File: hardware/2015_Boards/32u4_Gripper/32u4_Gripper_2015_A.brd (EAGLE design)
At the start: 31.8 x 55.9 mm, 20 parts, among them U1 SN74LS241DW, U2 XBEE-1B3

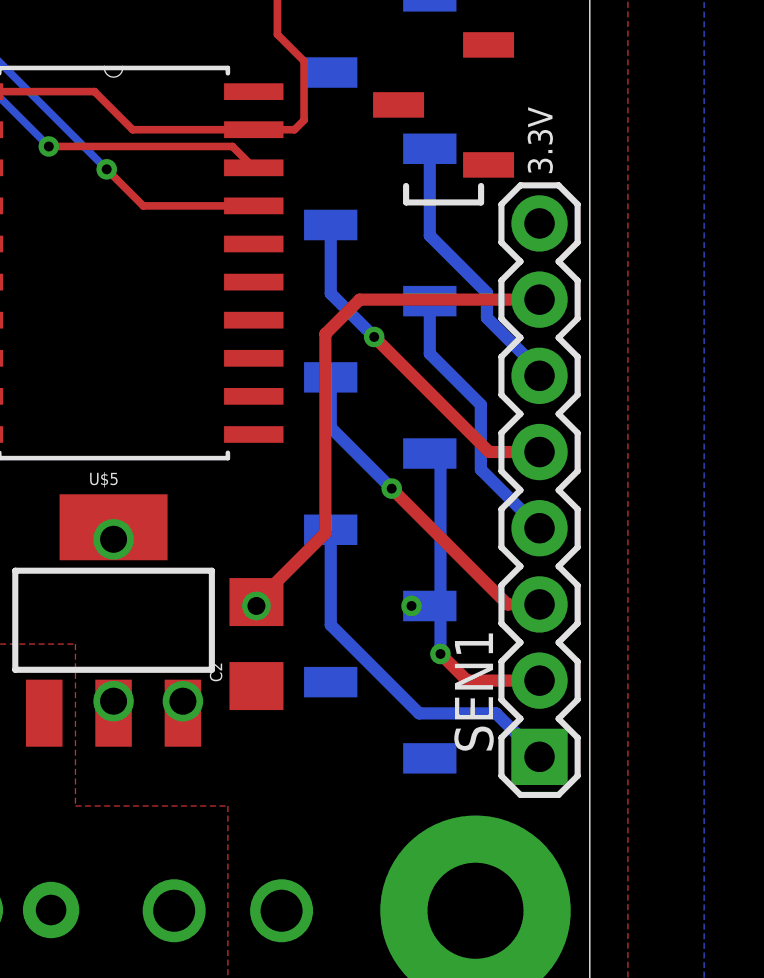
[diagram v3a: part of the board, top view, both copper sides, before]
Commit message: Cleaned up servo data trace
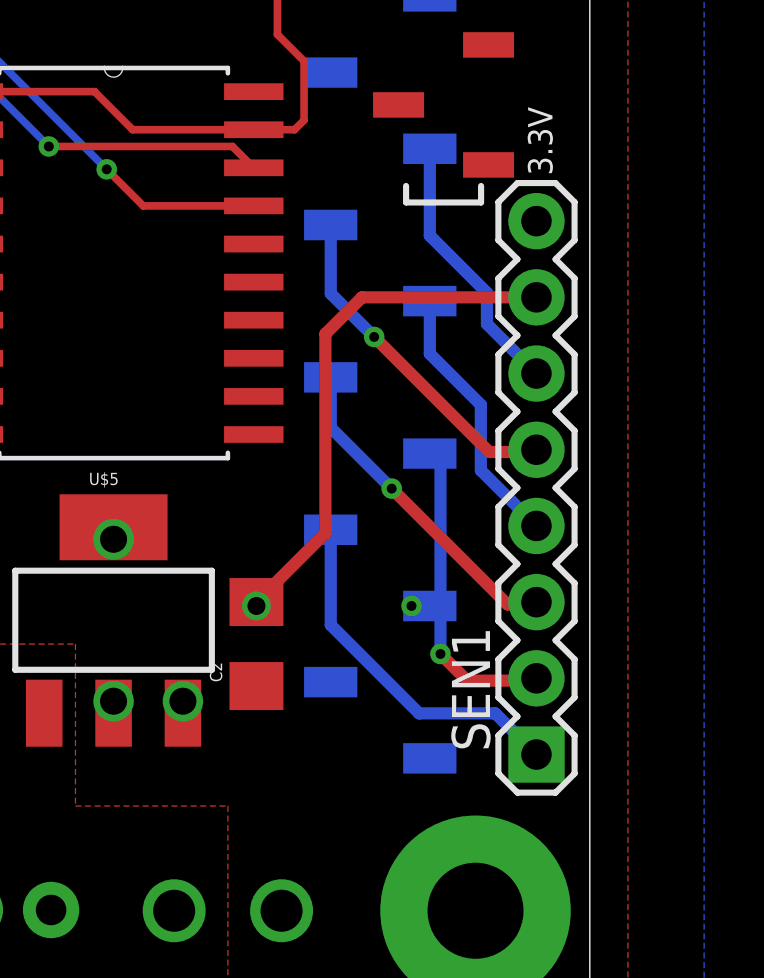
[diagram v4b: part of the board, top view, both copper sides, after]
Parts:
- moved SEN1 0.13 mm to (30.0, 9.02)
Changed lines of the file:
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@@
 <element name="C1" library="SparkFun-Passives" package="1206" value="0.1uF" x="11.1125" y="12.7" rot="R90"/>
 <element name="C2" library="SparkFun-Passives" package="1206" value="0.1uF" x="20.6375" y="12.7" rot="R90"/>
-<element name="SEN1" library="SparkFun-Connectors" package="1X08" value="" x="30.0736" y="8.9408" smashed="yes" rot="R90">
-<attribute name="NAME" x="28.5242" y="9.0424" size="1.27" layer="25" ratio="10" rot="R90"/>
-<attribute name="VALUE" x="33.2486" y="7.6708" size="1.27" layer="27" rot="R90"/>
+<element name="SEN1" library="SparkFun-Connectors" package="1X08" value="" x="29.972" y="9.017" smashed="yes" rot="R90">
+<attribute name="NAME" x="28.4226" y="9.1186" size="1.27" layer="25" ratio="10" rot="R90"/>
+<attribute name="VALUE" x="33.147" y="7.747" size="1.27" layer="27" rot="R90"/>
 </element>
 <element name="SEN2" library="SparkFun-Connectors" package="1X08" value="" x="1.8542" y="26.7462" smashed="yes" rot="R270">
@@
 <wire x1="20.6375" y1="14.1" x2="22.9362" y2="16.3987" width="0.4064" layer="1"/>
 <wire x1="22.9362" y1="16.3987" x2="22.9362" y2="23.0378" width="0.4064" layer="1"/>
-<wire x1="24.0792" y1="24.1808" x2="30.0736" y2="24.1808" width="0.4064" layer="1"/>
-<wire x1="22.9362" y1="23.0378" x2="24.0792" y2="24.1808" width="0.4064" layer="1"/>
+<wire x1="22.9362" y1="23.0378" x2="24.1554" y2="24.257" width="0.4064" layer="1"/>
+<wire x1="24.1554" y1="24.257" x2="29.972" y2="24.257" width="0.4064" layer="1"/>
 </signal>
 <signal name="RESET">
@@
 <contactref element="U$1" pad="P$4"/>
 <contactref element="SEN1" pad="1"/>
-<wire x1="30.0736" y1="8.9408" x2="28.6258" y2="10.3886" width="0.4064" layer="16"/>
 <wire x1="23.114" y1="13.335" x2="23.114" y2="16.51" width="0.4064" layer="16"/>
-<wire x1="28.6258" y1="10.3886" x2="26.0604" y2="10.3886" width="0.4064" layer="16"/>
 <wire x1="26.0604" y1="10.3886" x2="23.114" y2="13.335" width="0.4064" layer="16"/>
+<wire x1="26.0604" y1="10.3886" x2="28.6004" y2="10.3886" width="0.4064" layer="16"/>
+<wire x1="28.6004" y1="10.3886" x2="29.972" y2="9.017" width="0.4064" layer="16"/>
 </signal>
 <signal name="N$3">
 <contactref element="U$1" pad="P$5"/>
 <contactref element="SEN1" pad="2"/>
-<wire x1="30.0736" y1="11.4808" x2="27.6606" y2="11.4808" width="0.4064" layer="1"/>
 <wire x1="27.6606" y1="11.4808" x2="26.7716" y2="12.3698" width="0.4064" layer="1"/>
 <via x="26.7716" y="12.3698" extent="1-16" drill="0.3302"/>
 <wire x1="26.7716" y1="12.3698" x2="26.7716" y2="18.6944" width="0.4064" layer="16"/>
 <wire x1="26.7716" y1="18.6944" x2="26.416" y2="19.05" width="0.4064" layer="16"/>
+<wire x1="27.6606" y1="11.4808" x2="29.8958" y2="11.4808" width="0.4064" layer="1"/>
+<wire x1="29.8958" y1="11.4808" x2="29.972" y2="11.557" width="0.4064" layer="1"/>
 </signal>
 <signal name="N$5">
 <contactref element="U$1" pad="P$6"/>
 <contactref element="SEN1" pad="3"/>
-<wire x1="30.0736" y1="14.0208" x2="29.0068" y2="14.0208" width="0.4064" layer="1"/>
 <wire x1="29.0068" y1="14.0208" x2="25.146" y2="17.8816" width="0.4064" layer="1"/>
 <via x="25.146" y="17.8816" extent="1-16" drill="0.3302"/>
 <wire x1="25.146" y1="17.8816" x2="23.114" y2="19.9136" width="0.4064" layer="16"/>
 <wire x1="23.114" y1="19.9136" x2="23.114" y2="21.59" width="0.4064" layer="16"/>
+<wire x1="29.0068" y1="14.0208" x2="29.8958" y2="14.0208" width="0.4064" layer="1"/>
+<wire x1="29.8958" y1="14.0208" x2="29.972" y2="14.097" width="0.4064" layer="1"/>
 </signal>
 <signal name="N$6">
 <contactref element="SEN1" pad="4"/>
 <contactref element="U$1" pad="P$7"/>
-<wire x1="30.0736" y1="16.5608" x2="28.1178" y2="18.5166" width="0.4064" layer="16"/>
-<wire x1="28.1178" y1="18.5166" x2="28.1178" y2="20.6756" width="0.4064" layer="16"/>
+<wire x1="28.1178" y1="18.4912" x2="28.1178" y2="20.6756" width="0.4064" layer="16"/>
 <wire x1="28.1178" y1="20.6756" x2="26.416" y2="22.3774" width="0.4064" layer="16"/>
 <wire x1="26.416" y1="22.3774" x2="26.416" y2="24.13" width="0.4064" layer="16"/>
+<wire x1="28.1178" y1="18.4912" x2="29.972" y2="16.637" width="0.4064" layer="16"/>
 </signal>
 <signal name="N$7">
@@
 <via x="24.5618" y="22.9362" extent="1-16" drill="0.3302"/>
 <wire x1="24.5618" y1="22.9362" x2="28.3972" y2="19.1008" width="0.4064" layer="1"/>
-<wire x1="28.3972" y1="19.1008" x2="30.0736" y2="19.1008" width="0.4064" layer="1"/>
 <wire x1="24.5618" y1="22.9362" x2="23.114" y2="24.384" width="0.4064" layer="16"/>
 <wire x1="23.114" y1="24.384" x2="23.114" y2="26.67" width="0.4064" layer="16"/>
+<wire x1="28.3972" y1="19.1008" x2="29.8958" y2="19.1008" width="0.4064" layer="1"/>
+<wire x1="29.8958" y1="19.1008" x2="29.972" y2="19.177" width="0.4064" layer="1"/>
 </signal>
 <signal name="N$8">
@@
 <wire x1="26.416" y1="29.21" x2="26.416" y2="26.3144" width="0.4064" layer="16"/>
 <wire x1="26.416" y1="26.3144" x2="28.321" y2="24.4094" width="0.4064" layer="16"/>
-<wire x1="28.321" y1="24.4094" x2="28.321" y2="23.5712" width="0.4064" layer="16"/>
-<wire x1="28.321" y1="23.5712" x2="30.0736" y2="21.8186" width="0.4064" layer="16"/>
-<wire x1="30.0736" y1="21.8186" x2="30.0736" y2="21.6408" width="0.4064" layer="16"/>
+<wire x1="28.321" y1="24.4094" x2="28.321" y2="23.368" width="0.4064" layer="16"/>
+<wire x1="28.321" y1="23.368" x2="29.972" y2="21.717" width="0.4064" layer="16"/>
 </signal>
 <signal name="N$11">

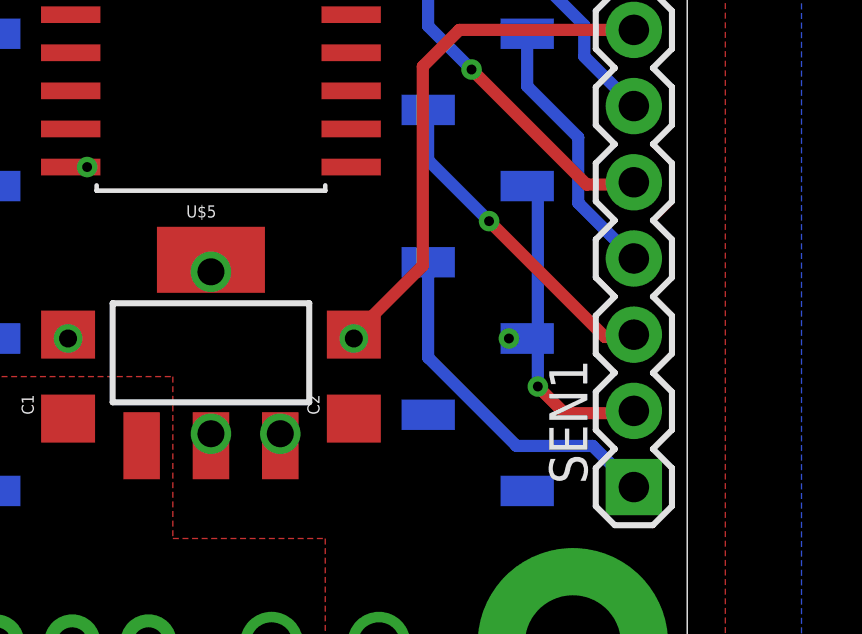
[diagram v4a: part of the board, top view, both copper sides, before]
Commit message: Fixed extra via
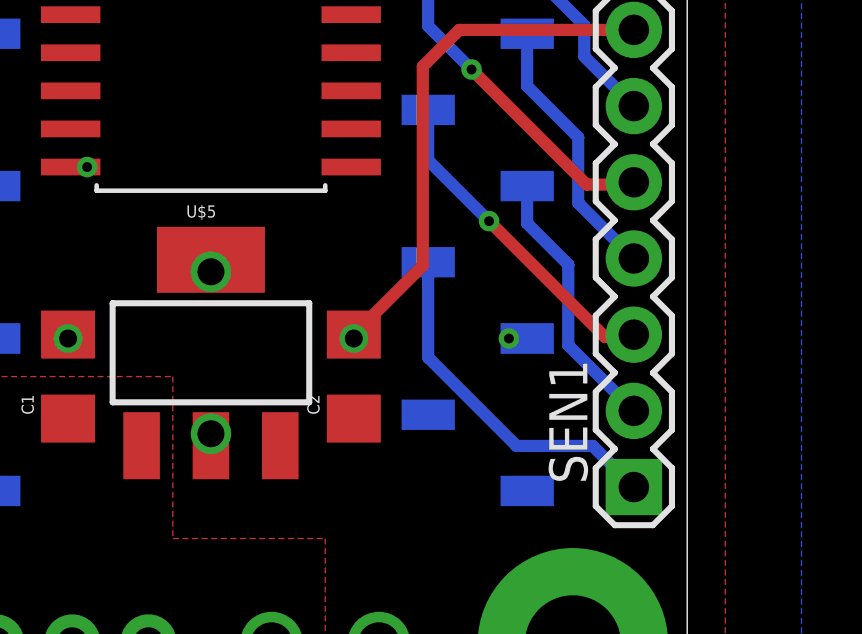
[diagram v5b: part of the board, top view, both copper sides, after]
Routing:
- net N$3: track 10.4 -> 8.97 mm, vias 1 -> 0
- net 3.3V: vias 2 -> 1
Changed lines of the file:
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@@
 <wire x1="31.75" y1="55.88" x2="0" y2="55.88" width="0" layer="20"/>
 <wire x1="0" y1="55.88" x2="0" y2="0" width="0" layer="20"/>
-<dimension x1="0" y1="55.88" x2="0" y2="0" x3="-5.08" y3="27.94" textsize="1.778" layer="25" unit="inch" precision="5"/>
-<dimension x1="0" y1="55.88" x2="31.75" y2="55.88" x3="15.875" y3="59.69" textsize="1.778" layer="25" unit="inch" precision="5"/>
 <text x="30.5054" y="28.321" size="0.8128" layer="21" rot="R90">3.3V</text>
 </plain>
@@
 <vertex x="33.02" y="-1.27"/>
 </polygon>
-<via x="18.1864" y="10.795" extent="1-16" drill="0.9" shape="square"/>
 <via x="25.8064" y="13.97" extent="1-16" drill="0.3302"/>
 <wire x1="25.8064" y1="13.97" x2="26.416" y2="13.97" width="0.3048" layer="16"/>
@@
 <contactref element="U$1" pad="P$5"/>
 <contactref element="SEN1" pad="2"/>
-<wire x1="27.6606" y1="11.4808" x2="26.7716" y2="12.3698" width="0.4064" layer="1"/>
-<via x="26.7716" y="12.3698" extent="1-16" drill="0.3302"/>
-<wire x1="26.7716" y1="12.3698" x2="26.7716" y2="18.6944" width="0.4064" layer="16"/>
-<wire x1="26.7716" y1="18.6944" x2="26.416" y2="19.05" width="0.4064" layer="16"/>
-<wire x1="27.6606" y1="11.4808" x2="29.8958" y2="11.4808" width="0.4064" layer="1"/>
-<wire x1="29.8958" y1="11.4808" x2="29.972" y2="11.557" width="0.4064" layer="1"/>
+<wire x1="29.972" y1="11.557" x2="27.7876" y2="13.7414" width="0.4064" layer="16"/>
+<wire x1="27.7876" y1="13.7414" x2="27.7876" y2="16.4338" width="0.4064" layer="16"/>
+<wire x1="27.7876" y1="16.4338" x2="26.416" y2="17.8054" width="0.4064" layer="16"/>
+<wire x1="26.416" y1="17.8054" x2="26.416" y2="19.05" width="0.4064" layer="16"/>
 </signal>
 <signal name="N$5">
